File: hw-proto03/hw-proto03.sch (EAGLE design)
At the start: 43 parts, among them IC1 TLV74333PDBVR, IC2 IR4427S, IC3 MCP2562T, IC5 IR4427S, J1 J12MM, J2 J5MM, J3 J12MM, J4 J7MM, Q1 SQJ147ELP-T1_GE3, Q2 SQJ147ELP-T1_GE3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

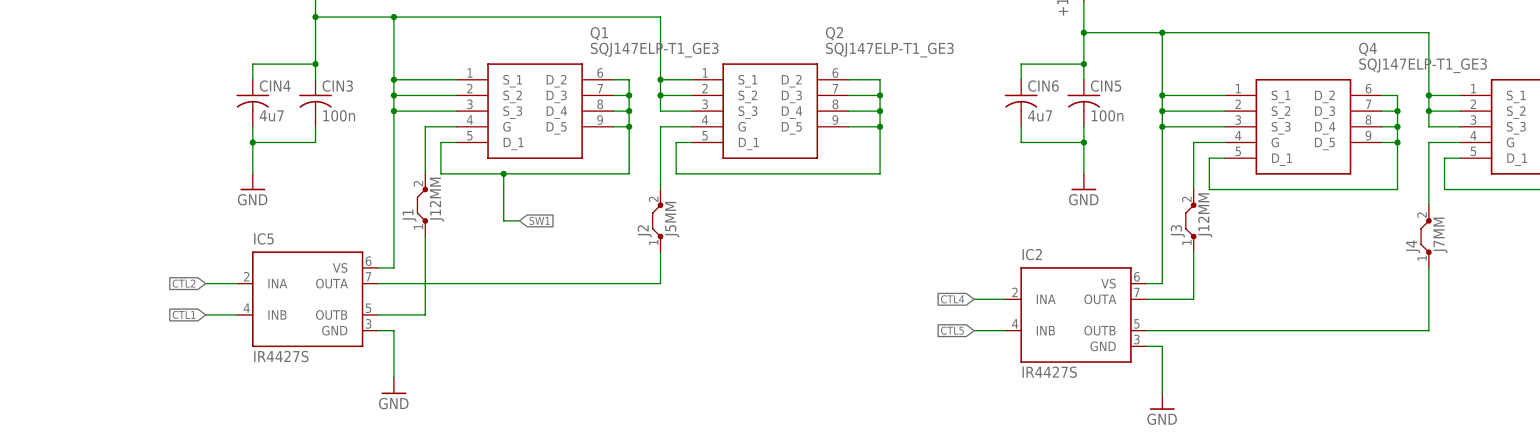
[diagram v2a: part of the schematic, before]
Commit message: updated new fet driver
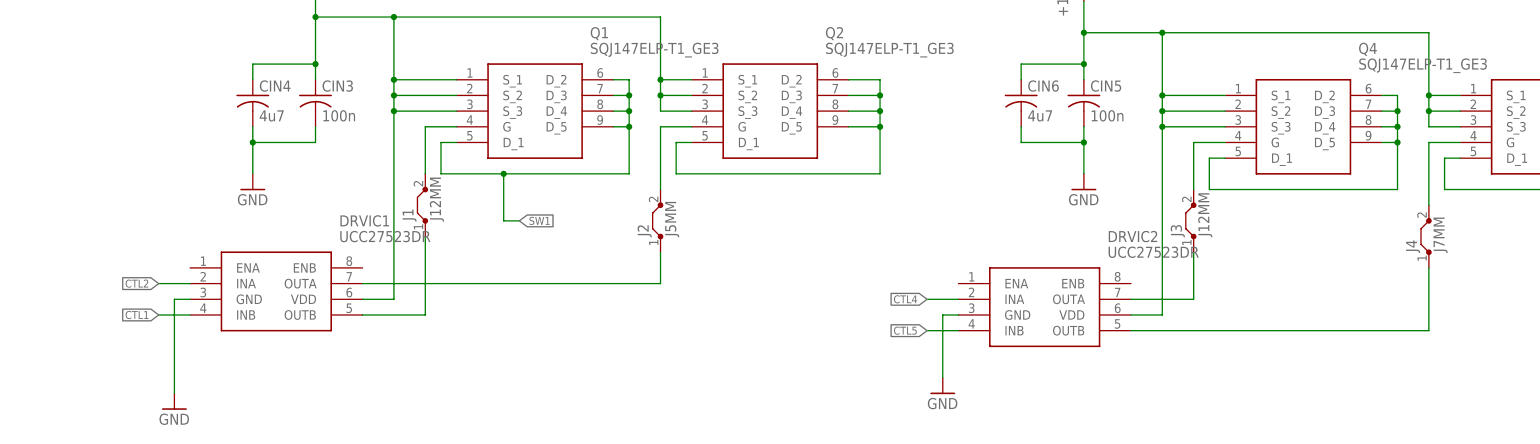
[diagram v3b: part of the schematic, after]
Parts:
- removed IC2, IC5: IR4427S, ir:IR4427S
- added DRVIC1, DRVIC2: UCC27523DR, UCC27523DR-fet-driver:UCC27523DR
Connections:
- net +12V: now also DRVIC1.VDD, DRVIC2.VDD; no longer IC2.VS, IC5.VS
- net CTL1: now also DRVIC1.INB; no longer IC5.INB
- net CTL2: now also DRVIC1.INA; no longer IC5.INA
- net CTL4: now also DRVIC2.INA; no longer IC2.INA
- net CTL5: now also DRVIC2.INB; no longer IC2.INB
- net GND: now also DRVIC1.GND, DRVIC2.GND; no longer IC2.GND, IC5.GND
- net N$13: now also DRVIC1.OUTA; no longer IC5.OUTA
- net N$4: now also DRVIC1.OUTB; no longer IC5.OUTB
- net N$8: now also DRVIC2.OUTB; no longer IC2.OUTB
- net N$9: now also DRVIC2.OUTA; no longer IC2.OUTA
